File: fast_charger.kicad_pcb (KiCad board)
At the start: 2 copper layers, 66.5 x 38.7 mm, 47 parts, among them J1 Screw_Terminal_01x02, J2 USB_A, J3 AVR-ISP-6, J4 Conn_02x08_Odd_Even, J5 Conn_02x03_Odd_Even, Q1 PJD25N03, Q2 PJD25N03, U1 CHY100, U2 IRS10752LVBF, U3 ATtiny404-SS, U4 AP7375, U5 AP7375, U6 INA180A4

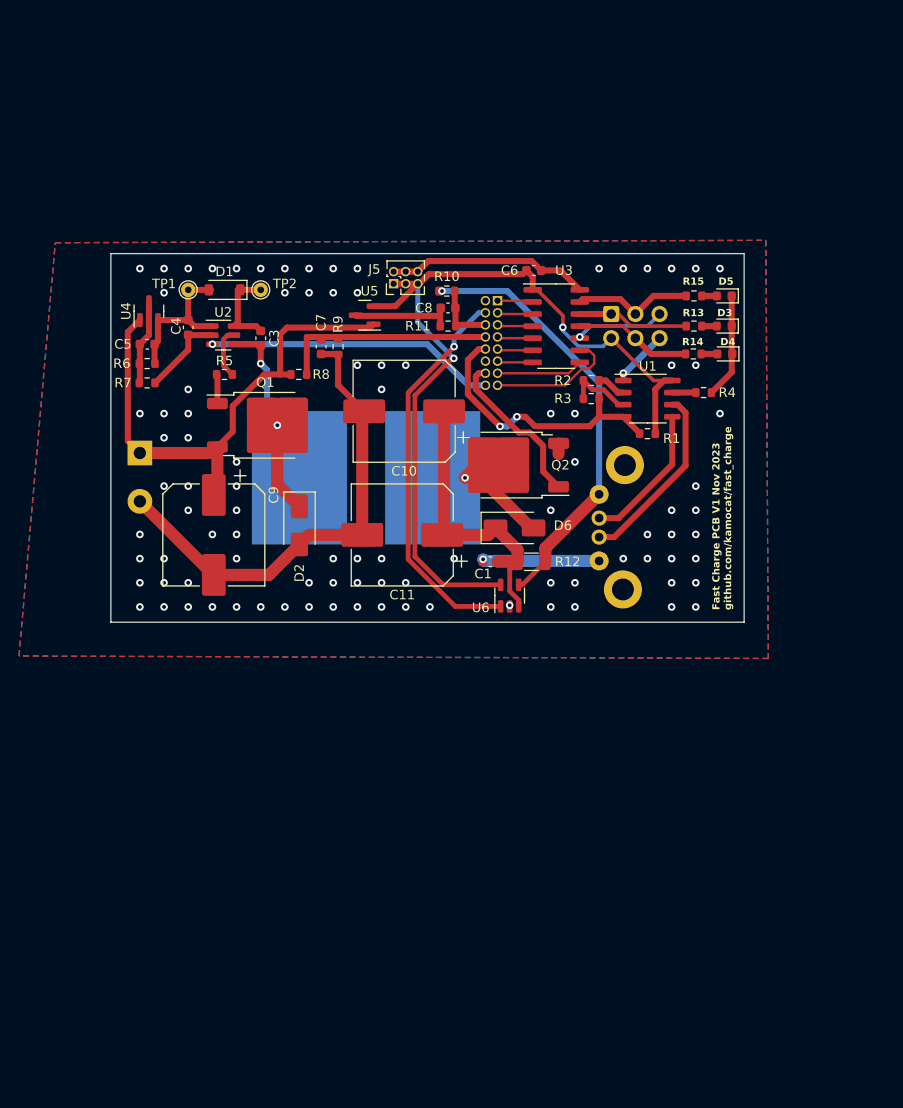
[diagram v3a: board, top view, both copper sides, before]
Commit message: New simpler buck-only design
Bridge rectifier on input to allow reverse voltage
Voltage regulation is taken care of by ASIC
External microcontroller and OLED display show power/voltage/current
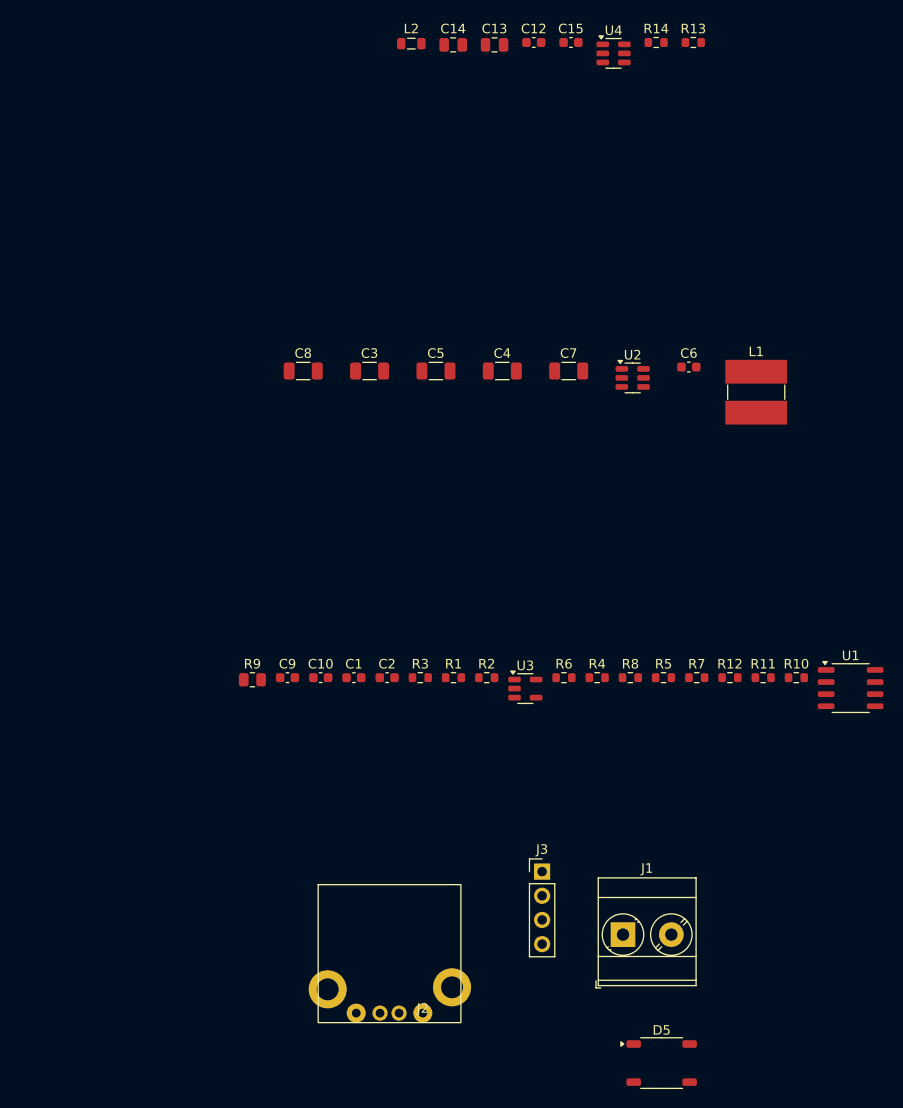
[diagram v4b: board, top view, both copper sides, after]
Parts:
- removed C11: 100u, Capacitor_SMD:CP_Elec_10x10.5
- removed D1: 1N4148W, Diode_SMD:D_SOD-123
- removed D2, D6: SBM54, Diode_SMD:D_SMA
- removed D3: RED, Diode_SMD:D_0603_1608Metric
- removed D4: YEL, Diode_SMD:D_0603_1608Metric
- removed J4: Conn_02x08_Odd_Even, Connector_PinHeader_1.27mm:PinHeader_2x08_P1.27mm_Vertical
- removed J5: Conn_02x03_Odd_Even, Connector_PinHeader_1.27mm:PinHeader_2x03_P1.27mm_Vertical
- removed Q1, Q2: PJD25N03, Package_TO_SOT_SMD:TO-252-2
- removed R15: 1k, Resistor_SMD:R_0603_1608Metric
- removed TP1, TP2: TestPoint, TestPoint:TestPoint_THTPad_D1.5mm_Drill0.7mm
- removed U5: AP7375, Package_TO_SOT_SMD:SOT-23
- removed U6: INA180A4, Package_TO_SOT_SMD:SOT-23-5
- added C12: 0.1u, Capacitor_SMD:C_0603_1608Metric, F.Cu at (103.6, 29.2)
- added C13: 10u, Capacitor_SMD:C_0805_2012Metric, F.Cu at (99.5, 29.5)
- added C14: 10u, Capacitor_SMD:C_0805_2012Metric, F.Cu at (95.2, 29.5)
- added C15: 47p, Capacitor_SMD:C_0603_1608Metric, F.Cu at (107.5, 29.2)
- added C2: 47p, Capacitor_SMD:C_0603_1608Metric, F.Cu at (88.2, 96.0)
- added L2: 10uH, Inductor_SMD:L_0805_2012Metric, F.Cu at (90.8, 29.4)
- C1: value 10n -> 0.22u
- C10, C9: value 100u -> 0.1u; footprint Capacitor_SMD:CP_Elec_10x10.5 -> Capacitor_SMD:C_0603_1608Metric
- C3, C4, C5, C7, C8: value 10n -> 10u; footprint Capacitor_SMD:C_0603_1608Metric -> Capacitor_SMD:C_1206_3216Metric
- C6: value 10n -> 0.1u
- D5: value GRN -> TS360ILS; footprint Diode_SMD:D_0603_1608Metric -> Package_SO:TSSOP-4_4.4x5mm_P4mm
- J1, J2: moved to F.Cu
- J3: value AVR-ISP-6 -> Conn_01x04_Socket; footprint Connector_IDC:IDC-Header_2x03_P2.54mm_Vertical -> Connector_PinHeader_2.54mm:PinHeader_1x04_P2.54mm_Vertical; moved to F.Cu
- L1: value 47u -> 3.3uH; footprint fast_charger:L_murata_6000B -> fast_charger:L_6.5x6.5; moved to F.Cu
- R1: value 400k -> 15.8k
- R10: value 400k -> 158k
- R11: value 100k -> 17.4k
- R12: value 20m -> 158k; footprint Resistor_SMD:R_1206_3216Metric -> Resistor_SMD:R_0603_1608Metric
- R13: value 1k -> 30.1k
- R14: value 1k -> 93.1k
- R2: value 100k -> 42.2k
- R3: value 100k -> 31.6k
- R5: value 10 -> 4.53k
- R6: value 4.7k -> 390k
- R7: value 10k -> 158k
- R8: value 400k -> 30.1k
- R9: value 100k -> 5m; footprint Resistor_SMD:R_0603_1608Metric -> Resistor_SMD:R_0805_2012Metric
- U2: value IRS10752LVBF -> AP63300WU; footprint Package_TO_SOT_SMD:SOT-23-6 -> Package_TO_SOT_SMD:TSOT-23-6
- U3: value ATtiny404-SS -> INA180A4; footprint Package_SO:SOIC-14_3.9x8.7mm_P1.27mm -> Package_TO_SOT_SMD:SOT-23-5
- U4: value AP7375 -> AP64060; footprint Package_TO_SOT_SMD:SOT-23 -> Package_TO_SOT_SMD:SOT-23-6
- moved D5 80.9 mm to (117.1, 136.5), turned to 0 degrees
- moved J1 71.7 mm to (113.0, 123.0), turned to 0 degrees
- moved R7 65.5 mm to (120.7, 96.0)
- moved J3 59.0 mm to (104.5, 116.4), turned to 0 degrees
- moved J2 57.6 mm to (92.0, 131.2), turned to 0 degrees
- moved R5 56.1 mm to (117.3, 96.0)
- moved U4 55.8 mm to (112.0, 30.4), turned to 0 degrees
- moved R6 54.8 mm to (106.8, 96.0), turned to 0 degrees
- moved R10 54.8 mm to (131.2, 96.0)
- moved R11 49.6 mm to (127.7, 96.0), turned to 0 degrees
- moved R8 47.2 mm to (113.8, 96.0)
- moved U2 43.3 mm to (114.0, 64.5)
- moved L1 42.0 mm to (127.0, 66.0)
- moved U3 38.2 mm to (102.7, 97.1)
- moved U1 37.1 mm to (136.9, 97.1)
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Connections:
- C1 pad 1: Net-(D6-K) -> GND
- C1 pad 2: GND -> Net-(U1-BP)
- C10 pad 1: Net-(D6-K) -> Net-(J3-Pin_2)
- C3 pad 1: Net-(D1-K) -> VDD
- C3 pad 2: /VSW -> GND
- C4 pad 1: Net-(D1-A) -> VBUS
- C5 pad 1: Net-(D1-A) -> VBUS
- C5 pad 2: Net-(U4-GND) -> GND
- C6 pad 1: +5V -> Net-(U2-SW)
- C6 pad 2: GND -> Net-(U2-BST)
- C7 pad 1: Net-(J4-Pin_8) -> VBUS
- C8 pad 1: Net-(J4-Pin_6) -> VBUS
- C9 pad 1: VDD -> Net-(J3-Pin_3)
- D5 pad 1: GND -> VDD
- D5 pad 2: Net-(D5-A) -> GND
- J1 pad 1: VDD -> Net-(J1-Pin_1)
- J1 pad 2: GND -> Net-(J1-Pin_2)
- J2 pad 1: VBUS -> Net-(J2-VBUS)
- J3 pad 1: /MISO -> +3.3V
- J3 pad 2: +5V -> Net-(J3-Pin_2)
- J3 pad 3: /SCK -> Net-(J3-Pin_3)
- J3 pad 4: /MOSI -> GND
- L1 pad 1: /VSW -> Net-(U2-SW)
- L1 pad 2: Net-(D6-A) -> VBUS
- R1 pad 1: /REQ_V -> /FB
- R1 pad 2: +5V -> Net-(U1-V3)
- R10 pad 2: Net-(J4-Pin_6) -> Net-(J3-Pin_3)
- R11 pad 1: Net-(J4-Pin_6) -> GND
- R11 pad 2: GND -> Net-(J3-Pin_3)
- R12 pad 1: Net-(D6-K) -> Net-(R12-Pad1)
- R12 pad 2: VBUS -> Net-(J3-Pin_2)
- R13 pad 1: /MISO -> Net-(U4-FB)
- R13 pad 2: Net-(D3-A) -> GND
- R14 pad 1: /MOSI -> +3.3V
- R14 pad 2: Net-(D4-A) -> Net-(U4-FB)
- R2 pad 1: Net-(U1-V1) -> /FB
- R3 pad 1: Net-(U1-V2) -> /FB
- R3 pad 2: /REQ_V -> Net-(U1-V1)
- R5 pad 1: Net-(Q1-G) -> Net-(U1-BP)
- R5 pad 2: Net-(U2-HO) -> VBUS
- R6 pad 1: Net-(D1-A) -> GND
- R6 pad 2: Net-(U4-GND) -> Net-(J2-D+)
- R7 pad 1: Net-(U4-GND) -> VBUS
- R7 pad 2: GND -> /FB
- R8 pad 1: VDD -> /FB
- R8 pad 2: Net-(J4-Pin_8) -> GND
- R9 pad 1: Net-(J4-Pin_8) -> VBUS
- R9 pad 2: GND -> Net-(J2-VBUS)
- U1 pad 4: /REQ_V -> Net-(U1-V3)
- U1 pad 8: +5V -> Net-(U1-BP)
- U2 pad 1: Net-(D1-A) -> /FB
- U2 pad 2: GND -> VDD
- U2 pad 3: /PWM -> VDD
- U2 pad 4: /VSW -> GND
- U2 pad 5: Net-(U2-HO) -> Net-(U2-SW)
- U2 pad 6: Net-(D1-K) -> Net-(U2-BST)
- U3 pad 1: +5V -> Net-(R12-Pad1)
- U3 pad 2: Net-(J4-Pin_1) -> GND
- U3 pad 3: Net-(J4-Pin_3) -> VBUS
- U3 pad 4: Net-(J4-Pin_5) -> Net-(J2-VBUS)
- U3 pad 5: Net-(J4-Pin_7) -> +3.3V
- U4 pad 1: VDD -> Net-(U4-BST)
- U4 pad 2: Net-(D1-A) -> GND
- U4 pad 3: Net-(U4-GND) -> Net-(U4-FB)
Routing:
- net GND: track 133.0 -> 0.00 mm, vias 96 -> 0
- net +5V: track 91.9 -> 0.00 mm, vias 2 -> 0
- net VDD: track 55.6 -> 0.00 mm
- net VBUS: track 46.1 -> 0.00 mm, vias 1 -> 0
- net /ILOAD: track 41.5 -> 0.00 mm, vias 1 -> 0
- net /VSW: track 32.5 -> 0.00 mm, vias 2 -> 0
- net Net-(D6-K): track 31.0 -> 0.00 mm
- net /PWM: track 30.5 -> 0.00 mm, vias 1 -> 0
- net /REQ_V: track 29.3 -> 0.00 mm, vias 2 -> 0
- net Net-(J4-Pin_8): track 22.7 -> 0.00 mm
- net Net-(J2-D+): track 19.5 -> 0.00 mm
- net /PWM2: track 17.0 -> 0.00 mm
- net Net-(D1-A): track 16.4 -> 0.00 mm
- net Net-(J2-D-): track 15.0 -> 0.00 mm
- net Net-(J4-Pin_15): track 13.7 -> 0.00 mm
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- removed copper zone on B.Cu, net GND
- removed copper zone on F.Cu, net GND
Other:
- board outline removed
- board text removed: "Fast Charge PCB V1 Nov 2023 github.com/kamocat/fast_charge"
